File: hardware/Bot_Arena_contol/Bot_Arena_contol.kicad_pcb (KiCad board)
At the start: 2 copper layers, 35 parts, among them J1 5Pin_5mm_plus_2.54_pin, J2 5Pin_5mm_plus_2.54_pin, J3 5Pin_5mm_plus_2.54_pin, J4 5Pin_5mm_plus_2.54_pin, J5 3Pin_5mm_plus_2.54_pin, J6 3Pin_5mm_plus_2.54_pin, J7 3Pin_5mm_plus_2.54_pin, Q1 IRLIZ44N, Q2 IRLIZ44N, Q3 IRLIZ44N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

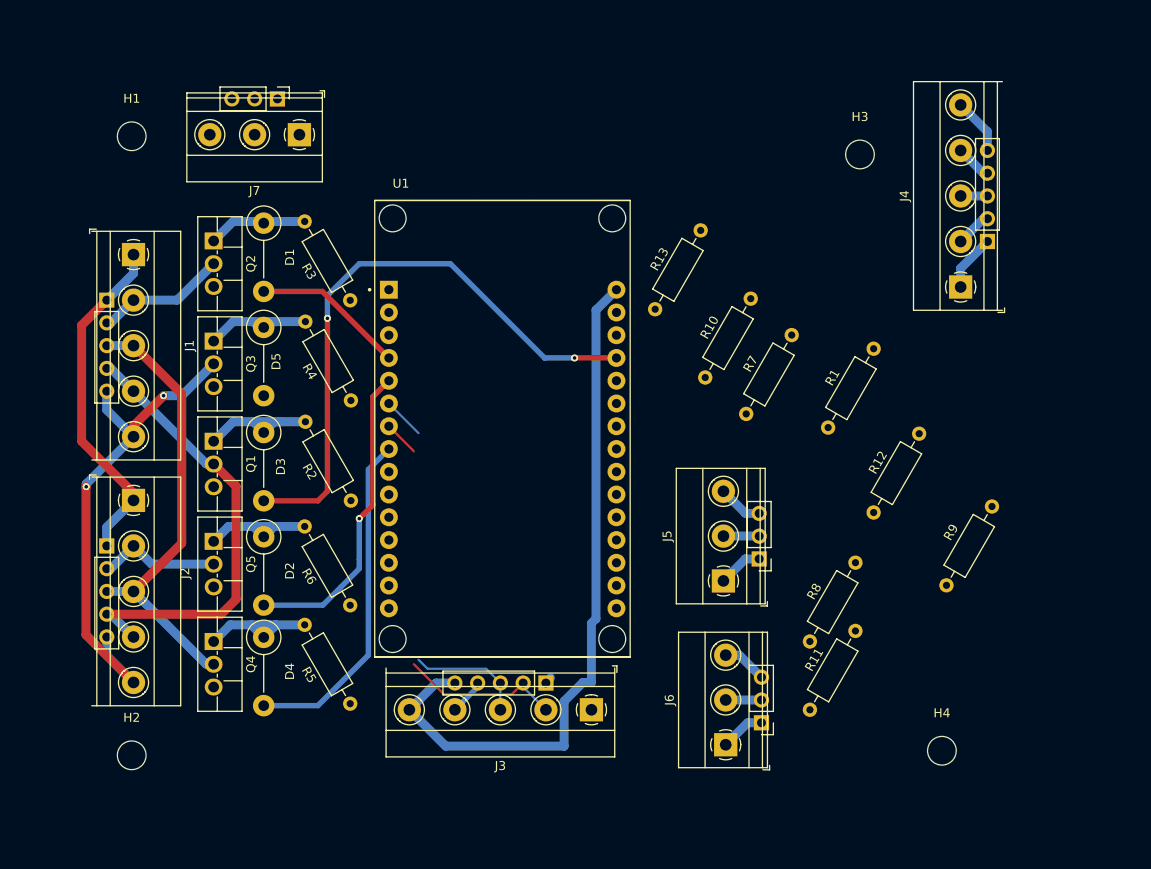
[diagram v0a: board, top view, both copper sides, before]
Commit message: Added cleaned up outline for now.  Still failing DRC, so we're not going to touch that atm.
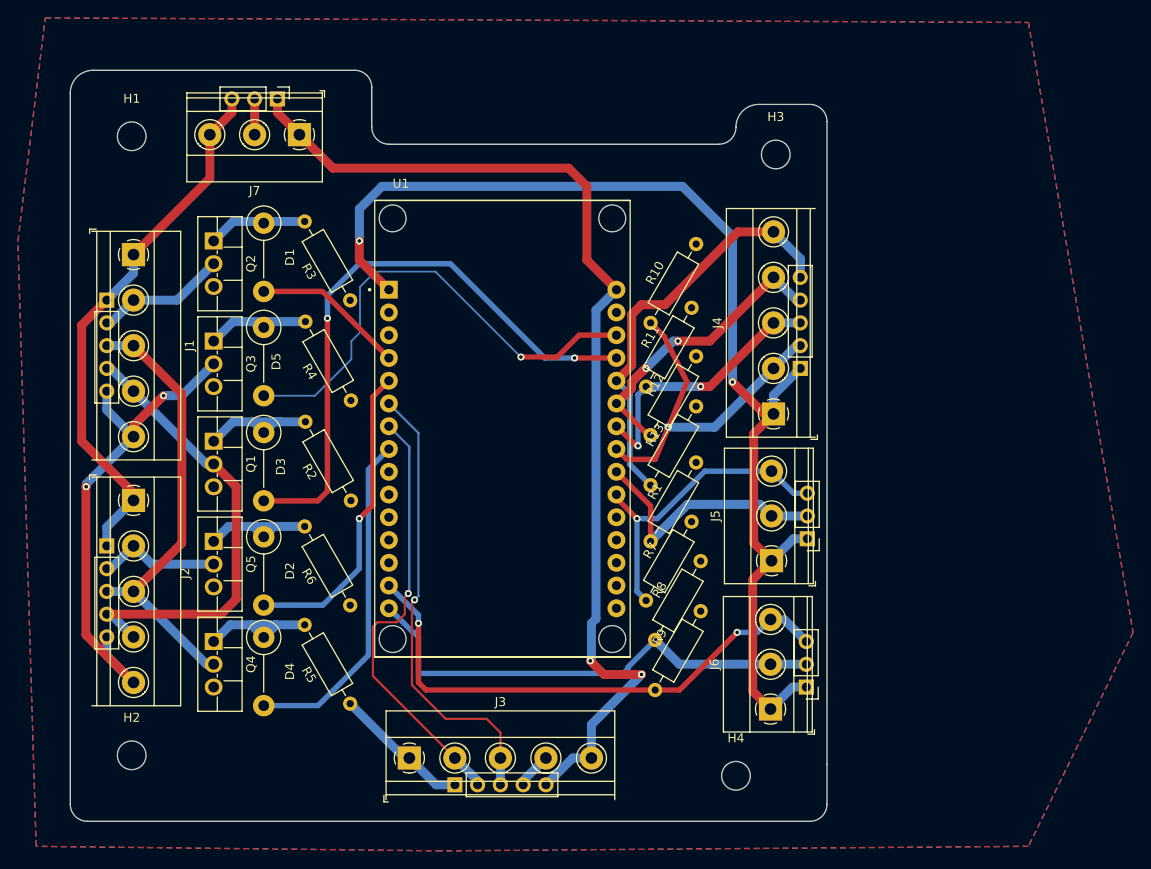
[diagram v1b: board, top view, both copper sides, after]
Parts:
- moved R11 40.4 mm to (88.4, 84.8)
- moved R9 34.5 mm to (89.4, 118.7)
- moved R12 26.3 mm to (88.9, 90.3)
- moved J4 25.2 mm to (102.6, 87.9)
- moved R7 23.6 mm to (88.4, 108.7)
- moved R1 23.5 mm to (88.9, 102.1)
- moved H4 23.2 mm to (98.4, 128.3)
- moved J3 21.0 mm to (62.0, 126.3), turned to 0 degrees
- moved R13 19.6 mm to (88.9, 95.8)
- moved R8 17.3 mm to (89.4, 113.1)
- moved H3 9.40 mm to (102.9, 58.9)
- moved R10 8.62 mm to (88.9, 77.7)
- moved J6 6.40 mm to (102.3, 120.8)
- moved J5 5.82 mm to (102.4, 104.3)
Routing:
- net +3V3: track 16.3 -> 130.4 mm, vias 0 -> 2
- net /m_Horn: track 0.00 -> 54.2 mm, vias 0 -> 1
- net /T_A_End: track 5.01 -> 58.6 mm, vias 0 -> 2
- net /T_A_Start: track 3.99 -> 54.7 mm
- net /G_Reset: track 6.32 -> 47.3 mm
- net +5V: track 79.2 -> 119.3 mm, vias 0 -> 3
- net /G_Start: track 4.04 -> 40.5 mm, vias 0 -> 1
- net /Dis_serial_Rx: track 17.9 -> 51.0 mm, vias 0 -> 1
- net /T_B_End: track 5.01 -> 35.4 mm, vias 0 -> 1
- net /G_Pause: track 2.99 -> 33.1 mm, vias 0 -> 2
- net /G_End: track 4.04 -> 33.1 mm, vias 0 -> 2
- net /Dis_Serial_Tx: track 22.5 -> 48.7 mm, vias 0 -> 1
- net /T_B_Start: track 3.99 -> 29.1 mm
- net +12V: track 38.5 -> 60.5 mm
- net GND: track 0.78 -> 19.4 mm
- added copper zone on B.Cu, net GND
- added copper zone on F.Cu, net GND
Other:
- board outline added: 84.5 x 83.8 mm

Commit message: Added pretty PCB version.
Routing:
- net +3V3: track 130.4 -> 127.1 mm
- net +5V: track 119.3 -> 117.6 mm
- net Net-(D3-Pad1): track 15.2 -> 16.8 mm
- net /m_Horn: track 54.2 -> 52.7 mm
- net /T_A_Start: track 54.7 -> 53.5 mm
- net /G_Reset: track 47.3 -> 46.2 mm
- net +12V: track 60.5 -> 59.3 mm
- net /G_Start: track 40.5 -> 39.3 mm
- net /Dis_serial_Rx: track 51.0 -> 49.9 mm
- net /m_Green: track 67.5 -> 66.4 mm
- net Net-(D5-Pad1): track 14.2 -> 15.2 mm
- net /s_Red_2: track 13.8 -> 13.0 mm
- net /s_Horn: track 57.5 -> 56.8 mm
- net /m_Yellow: track 38.0 -> 37.3 mm
- net /T_B_Start: track 29.1 -> 28.4 mm
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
